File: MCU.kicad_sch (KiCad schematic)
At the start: 47 parts, among them J2 USB_C_Receptacle_USB2.0, J3 Conn_01x03_Male, Q4 BC547, U2 LM1117-3.3, U3 W25Q64JVSSIQ, U4 RP2040, Y1 Crystal

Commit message: Done
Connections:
- net +3V3: now also D4.2 (A)
- net +5V: no longer D4.2 (A)
- net HAP_PWM: now reaches U4.29 (GPIO18)
- no-connect marks 25 -> 24
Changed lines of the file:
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@@
   (no_connect (at 151.13 71.12))
   (no_connect (at 151.13 81.28))
-  (no_connect (at 151.13 96.52))
   (no_connect (at 151.13 83.82))
   (wire (pts (xy 246.38 57.15) (xy 246.38 60.96))
@@
     (stroke (width 0) (type default))
   )
+  (wire (pts (xy 151.13 96.52) (xy 154.94 96.52))
+    (stroke (width 0) (type default))
+  )
   (wire (pts (xy 52.07 166.37) (xy 52.07 167.64))
     (stroke (width 0) (type default))
@@
     (effects (font (size 1.27 1.27)) (justify left bottom))
   )
+  (hierarchical_label "HAP_PWM" (shape output) (at 154.94 96.52 0) (fields_autoplaced)
+    (effects (font (size 1.27 1.27)) (justify left))
+  )
   (hierarchical_label "LED_PWM" (shape output) (at 154.94 99.06 0) (fields_autoplaced)
     (effects (font (size 1.27 1.27)) (justify left))
@@
     )
   )
+  (symbol (lib_id "power:+3V3") (at 58.42 44.45 90) (unit 1)
+    (in_bom yes) (on_board yes) (dnp no)
+    (property "Reference" "#PWR034" (at 62.23 44.45 0)
+      (effects (font (size 1.27 1.27)) hide)
+    )
+    (property "Value" "+3V3" (at 54.61 46.99 0)
+      (effects (font (size 1.27 1.27)) (justify left))
+    )
+    (property "Footprint" "" (at 58.42 44.45 0)
+      (effects (font (size 1.27 1.27)) hide)
+    )
+    (property "Datasheet" "" (at 58.42 44.45 0)
+      (effects (font (size 1.27 1.27)) hide)
+    )
+    (pin "1")
+    (instances
+      (project "V2_Main"
+        (path "/2426fb93-57a0-4a38-a355-1b8504d03262/811f6d49-44ef-446a-a262-9e00ea03fcb8"
+          (reference "#PWR034") (unit 1)
+        )
+      )
+      (project "V3_Main"
+        (path "/34608048-0348-41a9-a792-f9741d67937a/b079f921-e296-417c-8081-ff257ef2f91a"
+          (reference "#PWR044") (unit 1)
+        )
+      )
+      (project "Light-CC"
+        (path "/a3254443-8240-44f0-af35-274db02f779b/04c702c6-04db-4682-92c6-1d956531dc1e"
+          (reference "#PWR048") (unit 1)
+        )
+      )
+      (project "V1_Main"
+        (path "/e63e39d7-6ac0-4ffd-8aa3-1841a4541b55/f711db5e-77b0-4494-90e8-aecb55e572ba"
+          (reference "#PWR023") (unit 1)
+        )
+      )
+    )
+  )
   (symbol (lib_id "power:GND") (at 34.29 190.5 0) (unit 1)
     (in_bom yes) (on_board yes) (dnp no) (fields_autoplaced)
@@
         )
       )
-    )
-  )
-  (symbol (lib_id "power:+5V") (at 58.42 44.45 90) (unit 1)
-    (in_bom yes) (on_board yes) (dnp no)
-    (property "Reference" "#PWR025" (at 62.23 44.45 0)
-      (effects (font (size 1.27 1.27)) hide)
-    )
-    (property "Value" "+5V" (at 58.42 41.91 90)
-      (effects (font (size 1.27 1.27)) (justify left))
-    )
-    (property "Footprint" "" (at 58.42 44.45 0)
-      (effects (font (size 1.27 1.27)) hide)
-    )
-    (property "Datasheet" "" (at 58.42 44.45 0)
-      (effects (font (size 1.27 1.27)) hide)
-    )
-    (pin "1")
-    (instances
-      (project "V2_Main"
-        (path "/2426fb93-57a0-4a38-a355-1b8504d03262/811f6d49-44ef-446a-a262-9e00ea03fcb8"
-          (reference "#PWR025") (unit 1)
-        )
-      )
-      (project "V3_Main"
-        (path "/34608048-0348-41a9-a792-f9741d67937a/b079f921-e296-417c-8081-ff257ef2f91a"
-          (reference "#PWR055") (unit 1)
-        )
-      )
-      (project "Light-CC"
-        (path "/a3254443-8240-44f0-af35-274db02f779b/04c702c6-04db-4682-92c6-1d956531dc1e"
-          (reference "#PWR013") (unit 1)
-        )
-      )
-      (project "V1_Main"
-        (path "/e63e39d7-6ac0-4ffd-8aa3-1841a4541b55/f711db5e-77b0-4494-90e8-aecb55e572ba"
-          (reference "#PWR09") (unit 1)
-        )
-      )

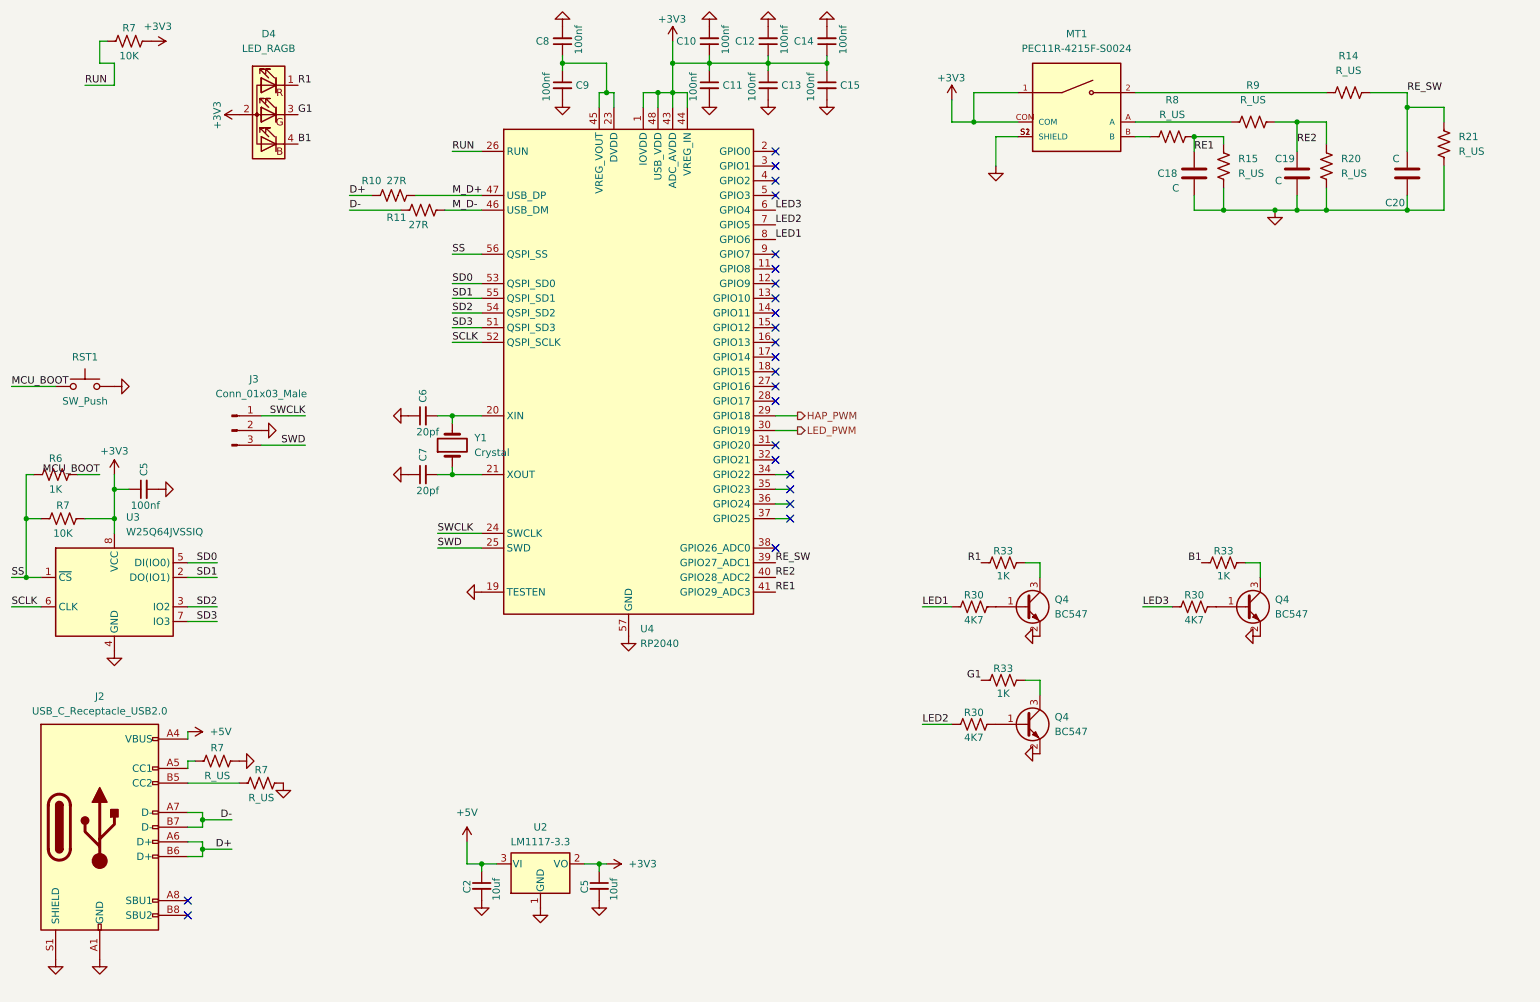
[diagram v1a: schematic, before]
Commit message: Changed the layout based on Power supply
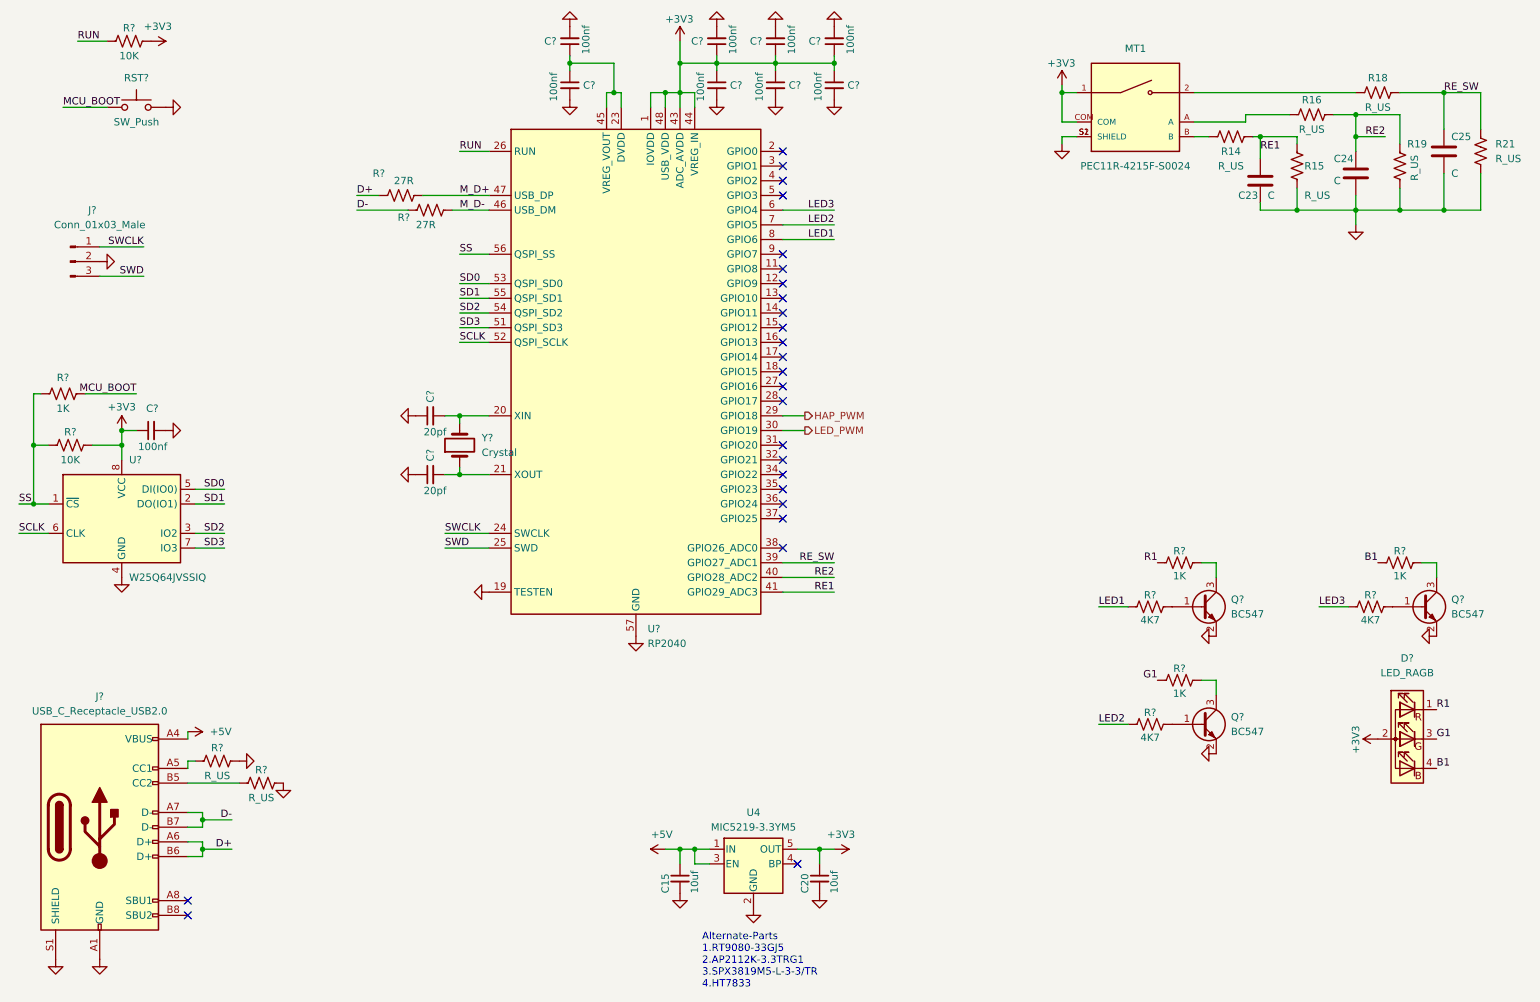
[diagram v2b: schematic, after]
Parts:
- removed C2, C5: 10uf, Capacitor_SMD:C_0805_2012Metric, symbol Device:C_Small
- removed U2: LM1117-3.3, Package_TO_SOT_SMD:SOT-223-3_TabPin2, symbol Regulator_Linear:LM1117-3.3
- added C15, C20: 10uf, Capacitor_SMD:C_0805_2012Metric, symbol Device:C_Small
- added U4: MIC5219-3.3YM5, Package_TO_SOT_SMD:SOT-23-5, symbol Regulator_Linear:MIC5219-3.3YM5
- C23: renamed from C18; footprint Capacitor_SMD:C_0603_1608Metric_Pad1.08x0.95mm_HandSolder -> Capacitor_SMD:C_0603_1608Metric
- C24: renamed from C19; footprint Capacitor_SMD:C_0603_1608Metric_Pad1.08x0.95mm_HandSolder -> Capacitor_SMD:C_0603_1608Metric
- C25: renamed from C20; footprint Capacitor_SMD:C_0603_1608Metric_Pad1.08x0.95mm_HandSolder -> Capacitor_SMD:C_0603_1608Metric
- MT1: footprint Rotary:XDCR_PEC11R-4215F-S0024 -> Rotary_Encoder:RotaryEncoder_Alps_EC11E_Vertical_H20mm
- R14: renamed from R8; footprint Resistor_SMD:R_0603_1608Metric_Pad0.98x0.95mm_HandSolder -> Resistor_SMD:R_0603_1608Metric
- R15, R21: footprint Resistor_SMD:R_0603_1608Metric_Pad0.98x0.95mm_HandSolder -> Resistor_SMD:R_0603_1608Metric
- R16: renamed from R9; footprint Resistor_SMD:R_0603_1608Metric_Pad0.98x0.95mm_HandSolder -> Resistor_SMD:R_0603_1608Metric
- R18: renamed from R14; footprint Resistor_SMD:R_0603_1608Metric_Pad0.98x0.95mm_HandSolder -> Resistor_SMD:R_0603_1608Metric
- R19: renamed from R20; footprint Resistor_SMD:R_0603_1608Metric_Pad0.98x0.95mm_HandSolder -> Resistor_SMD:R_0603_1608Metric
- U?: renamed from U4; footprint RP2040:QFN-56-1EP_7x7mm_P0.4mm_EP5.6x5.6mm_copy -> Package_DFN_QFN:QFN-56-1EP_7x7mm_P0.4mm_EP3.2x3.2mm
- renumbered C10 to C?, C8 to C?, C13 to C?, C6 to C?, C12 to C?, C7 to C?, C11 to C?, C9 to C?, C14 to C?, C15 to C?, C5 to C?, D4 to D?, J3 to J?, J2 to J?, Q4 to Q?, R33 to R?, R11 to R?, R6 to R?, R7 to R?, R30 to R?, R10 to R?, RST1 to RST?, U3 to U?, Y1 to Y?
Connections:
- net +3V3: now also C20.1, U4.5 (OUT)
- net +5V: now also C15.1, U4.1 (IN), U4.3 (EN)
- net GND: now also C15.2, C20.2, U4.2 (GND)
- no-connect marks 24 -> 25
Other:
- note added: "Alternate-Parts 1.RT9080-33GJ5 2.AP2112K-3.3TRG1 3.SPX3819M5-L-3-3/TR 4.HT7833"
- moved on the sheet: C23, C24, C25, C?, D?, J?, MT1, Q?, R14, R15, R16, R18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
